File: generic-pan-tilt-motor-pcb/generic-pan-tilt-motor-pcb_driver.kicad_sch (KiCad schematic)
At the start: 19 parts, among them Q1 DMN6075S, U1 TMC5240ATJ+

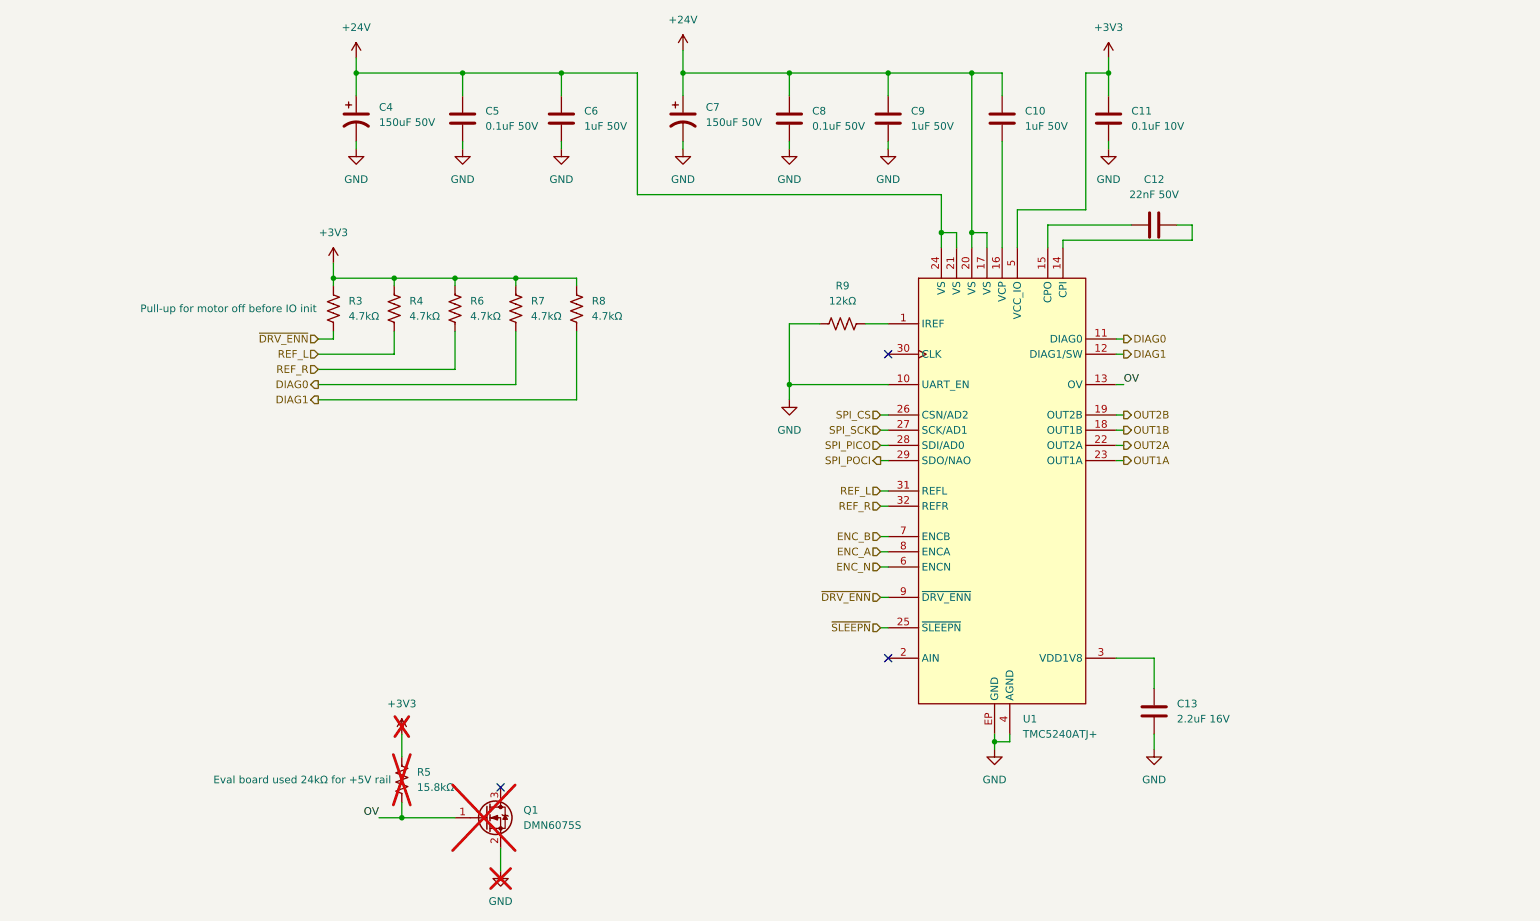
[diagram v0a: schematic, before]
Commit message: motor pcb all footprints, ov circuit
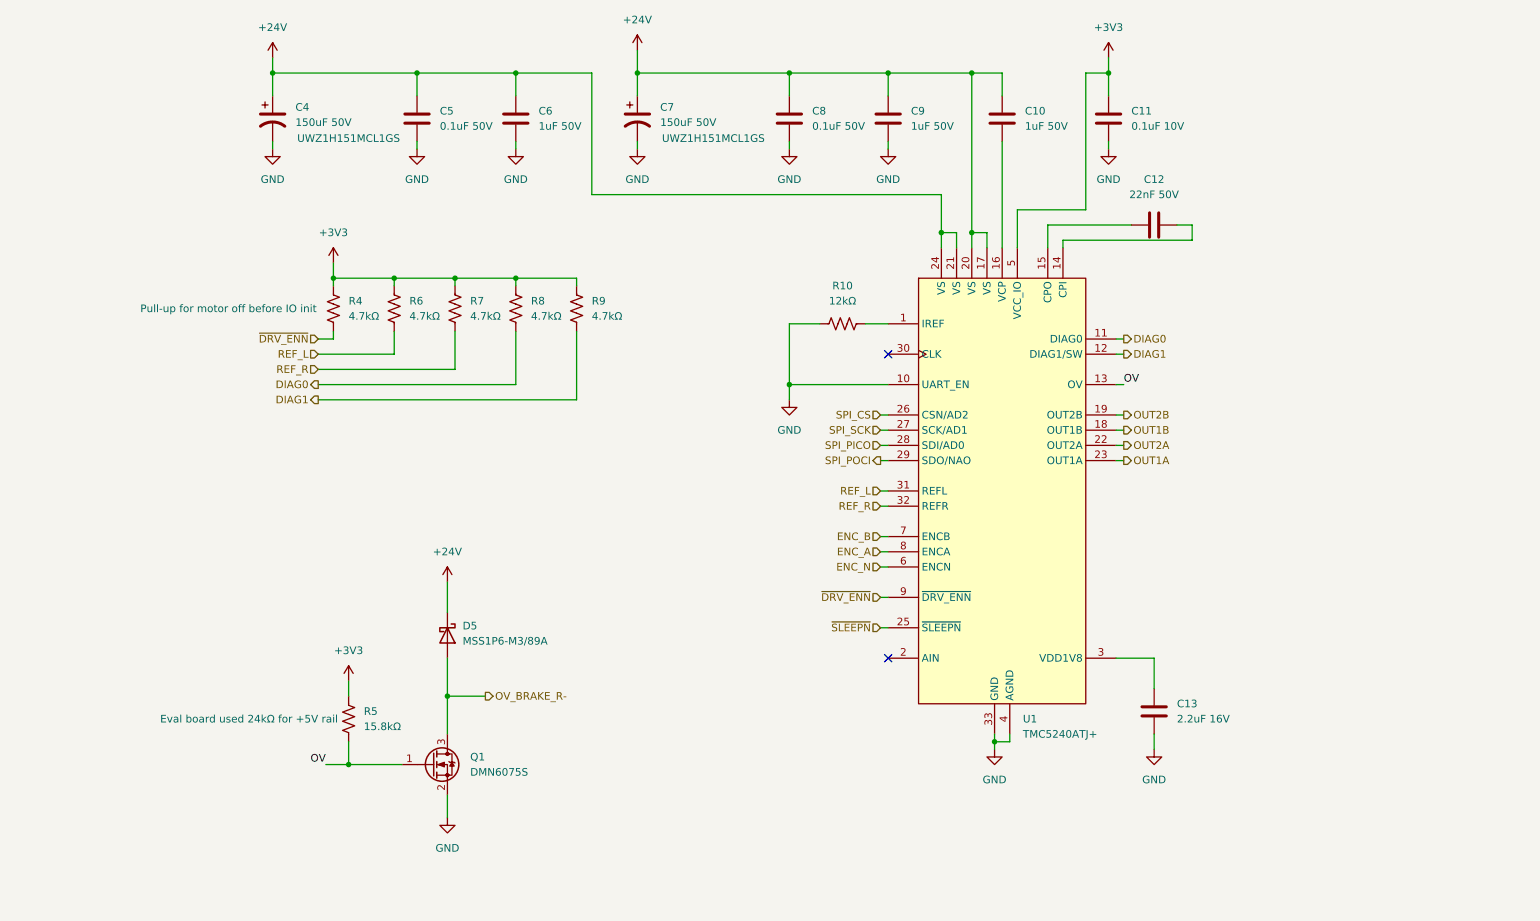
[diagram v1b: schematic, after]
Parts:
- added D5: MSS1P6-M3/89A, Diode_SMD:D_MicroSMP_AK, symbol Device:D_Schottky
- C10, C11, C12, C13, C5, C6, C8, C9: footprint (none) -> Capacitor_SMD:C_0603_1608Metric
- C4, C7: footprint (none) -> Capacitor_SMD:CP_Elec_10x10; digikey# (none) -> 493-9939-1-ND; manf# (none) -> UWZ1H151MCL1GS; mouser# (none) -> 647-UWZ1H151MCL1
- Q1: digikey# (none) -> DMN6075S-7DICT-ND; manf# (none) -> DMN6075S-7; mouser# (none) -> 621-DMN6075S-7; now fitted; now in the parts list
- R10: renamed from R9; footprint (none) -> Resistor_SMD:R_0402_1005Metric
- R4: renamed from R3; footprint (none) -> Resistor_SMD:R_0402_1005Metric
- R5: footprint (none) -> Resistor_SMD:R_0402_1005Metric; now fitted; now in the parts list
- R6: renamed from R4; footprint (none) -> Resistor_SMD:R_0402_1005Metric
- R7: renamed from R6; footprint (none) -> Resistor_SMD:R_0402_1005Metric
- R8: renamed from R7; footprint (none) -> Resistor_SMD:R_0402_1005Metric
- R9: renamed from R8; footprint (none) -> Resistor_SMD:R_0402_1005Metric
- U1: digikey# (none) -> 505-TMC5240ATJ+-ND; manf# (none) -> TMC5240ATJ+; mouser# (none) -> 700-TMC5240ATJ+
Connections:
- net +24V: now also D5.1 (K)
- net GND: now also U1.33 (GND); no longer U1.EP (GND)
- net OV_BRAKE_R-: now reaches Q1.3 (D)
- net OV_BRAKE_R-: now also D5.2 (A)
- no-connect marks 3 -> 2
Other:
- moved on the sheet: C4, C5, C6

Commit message: motor basic layout
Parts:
- added C14, C15, C16, C17: 1nF 100V, Capacitor_SMD:C_0603_1608Metric, symbol Device:C
- C11: value 0.1uF 10V -> 0.1uF 16V
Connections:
- net GND: now also C14.2, C15.2, C16.2, C17.2
- net OUT1A: now also C17.1
- net OUT1B: now also C15.1
- net OUT2A: now also C16.1
- net OUT2B: now also C14.1
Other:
- moved on the sheet: C10, C11, C12, C13, C4, C5, C6, C7, C8, C9, D5, Q1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

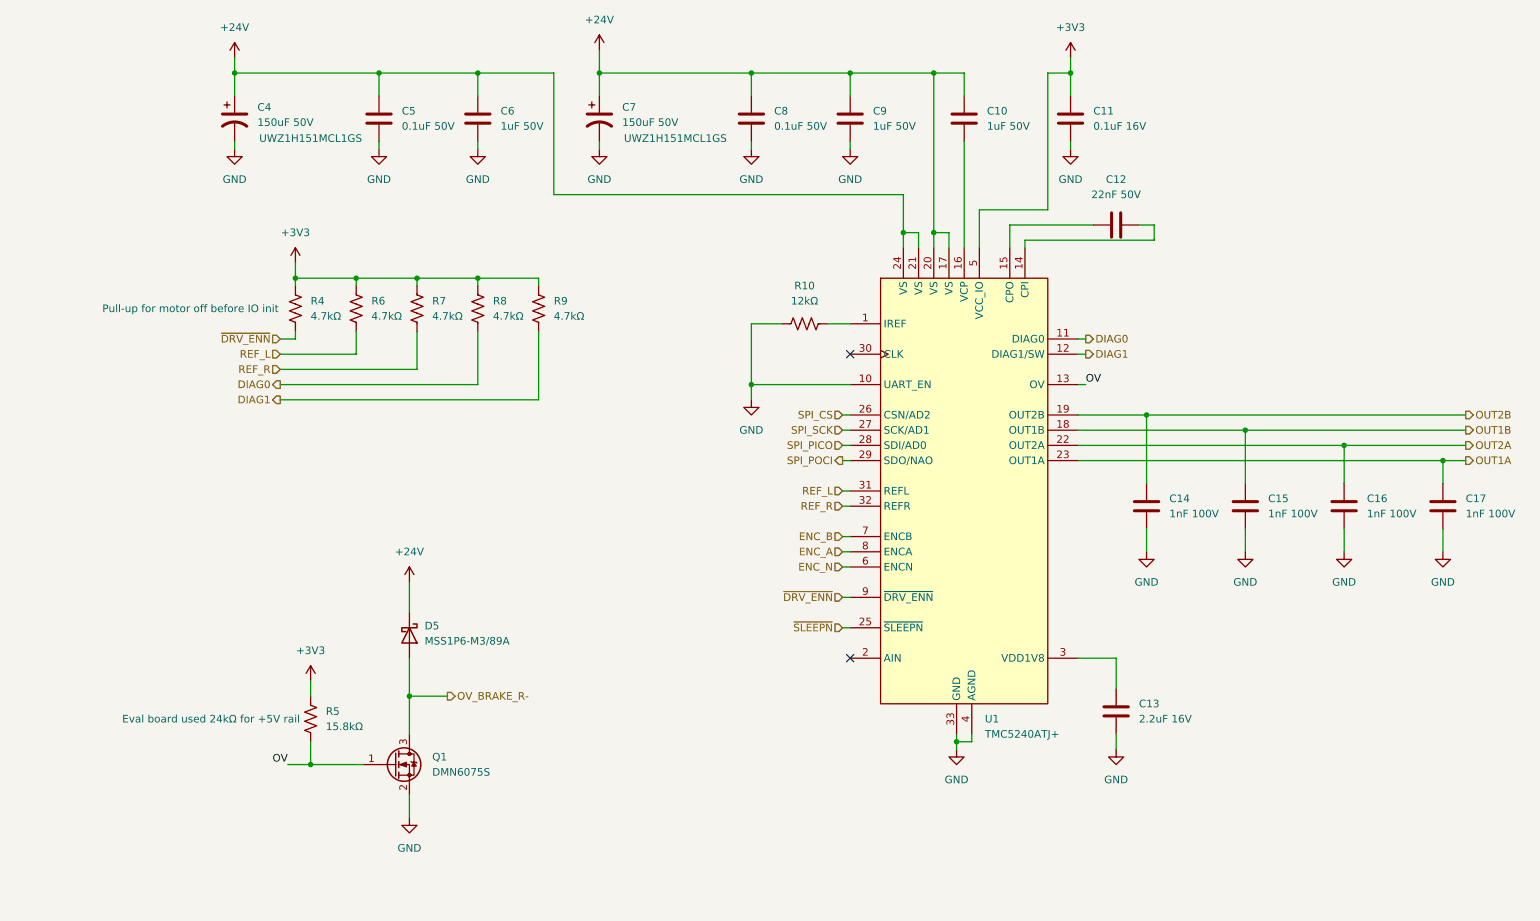
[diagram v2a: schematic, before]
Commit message: fix part numbers, add newark parts, separate fields for part desc
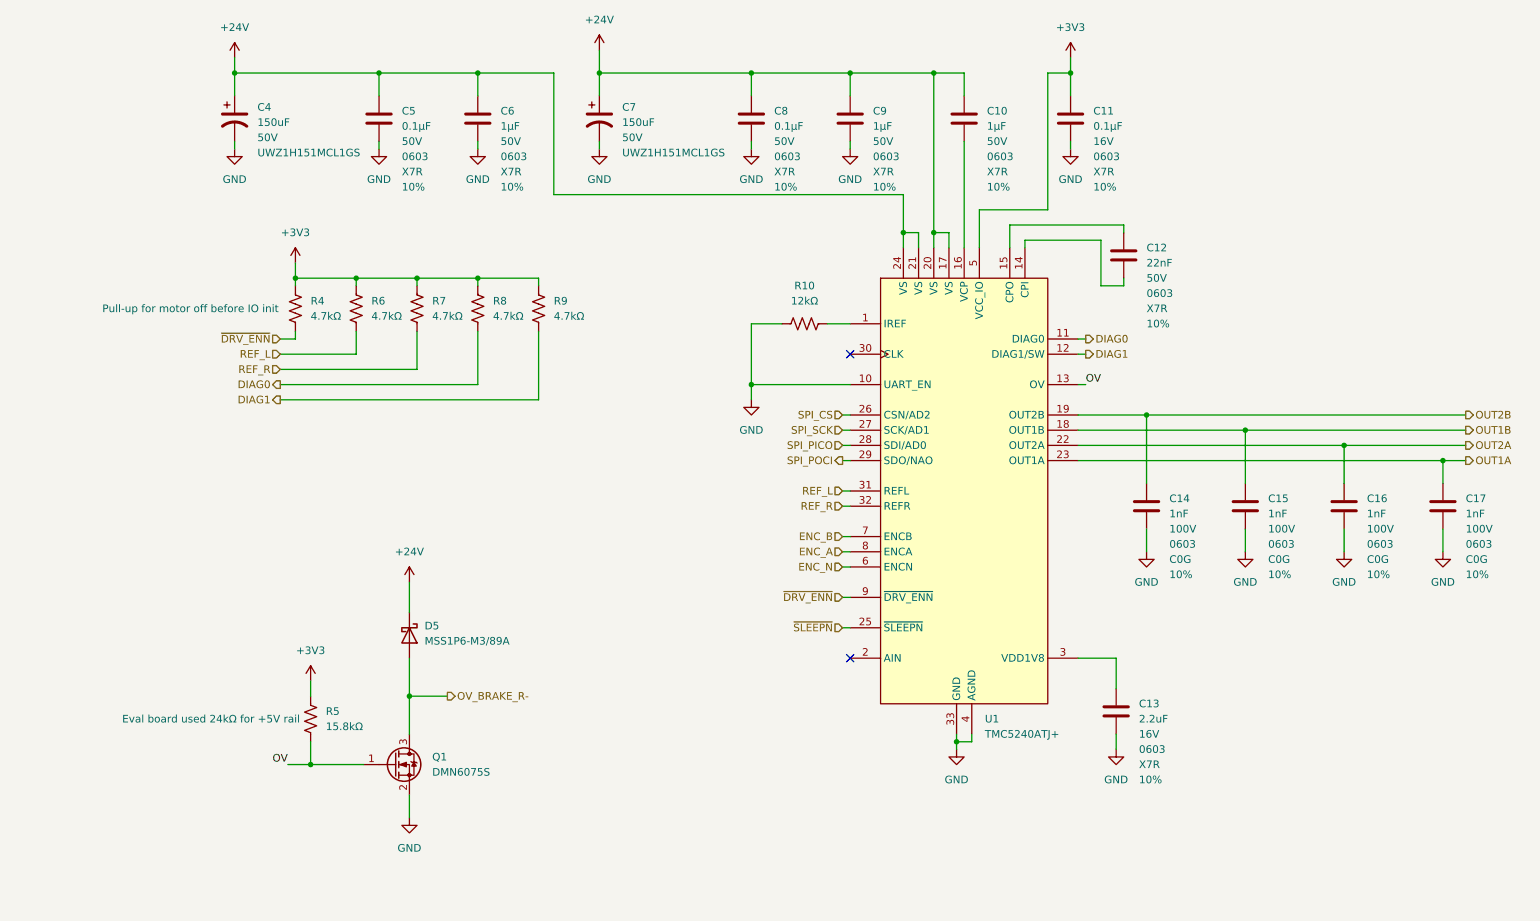
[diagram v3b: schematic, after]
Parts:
- C10, C6, C9: value 1uF 50V -> 1µF; Case Code (none) -> 0603; Dielectric (none) -> X7R; Tolerance (none) -> 10%; Voltage (none) -> 50V; manf# (none) -> CL10B105KB8NQNC; mouser# (none) -> 187­-CL10B105KB8NQNC
- C11: value 0.1uF 16V -> 0.1µF; Case Code (none) -> 0603; Dielectric (none) -> X7R; Tolerance (none) -> 10%; Voltage (none) -> 16V; manf# (none) -> CL10B104KO8NFNC; mouser# (none) -> 187-CL10B104KO8NFNC
- C12: value 22nF 50V -> 22nF; Case Code (none) -> 0603; Dielectric (none) -> X7R; Tolerance (none) -> 10%; Voltage (none) -> 50V; manf# (none) -> CL10B223KB8NNND; mouser# (none) -> 187-CL10B223KB8NNND
- C13: value 2.2uF 16V -> 2.2uF; Case Code (none) -> 0603; Dielectric (none) -> X7R; Tolerance (none) -> 10%; Voltage (none) -> 16V; manf# (none) -> GRM188Z71C225KE43D; mouser# (none) -> 81-­GRM188Z71C225KE3D
- C14, C15, C16, C17: value 1nF 100V -> 1nF; Case Code (none) -> 0603; Dielectric (none) -> C0G; Tolerance (none) -> 10%; Voltage (none) -> 100V; manf# (none) -> C0603C102K1GECTU; mouser# (none) -> 80­-C0603C102K1GEC
- C4, C7: value 150uF 50V -> 150uF; Voltage (none) -> 50V; newark# (none) -> 58R8961
- C5, C8: value 0.1uF 50V -> 0.1µF; Case Code (none) -> 0603; Dielectric (none) -> X7R; Tolerance (none) -> 10%; Voltage (none) -> 50V; manf# (none) -> CL10B104KB8NNNC; mouser# (none) -> 187-­CL10B104KB8NNNC
- D5: newark# (none) -> 75R2576
- Q1: newark# (none) -> 07AH3784
- U1: newark# (none) -> 69AK0101

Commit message: motor fix flipped spi mcp, spi tristate for drc, silk screw terminals, all parts manf and vendors
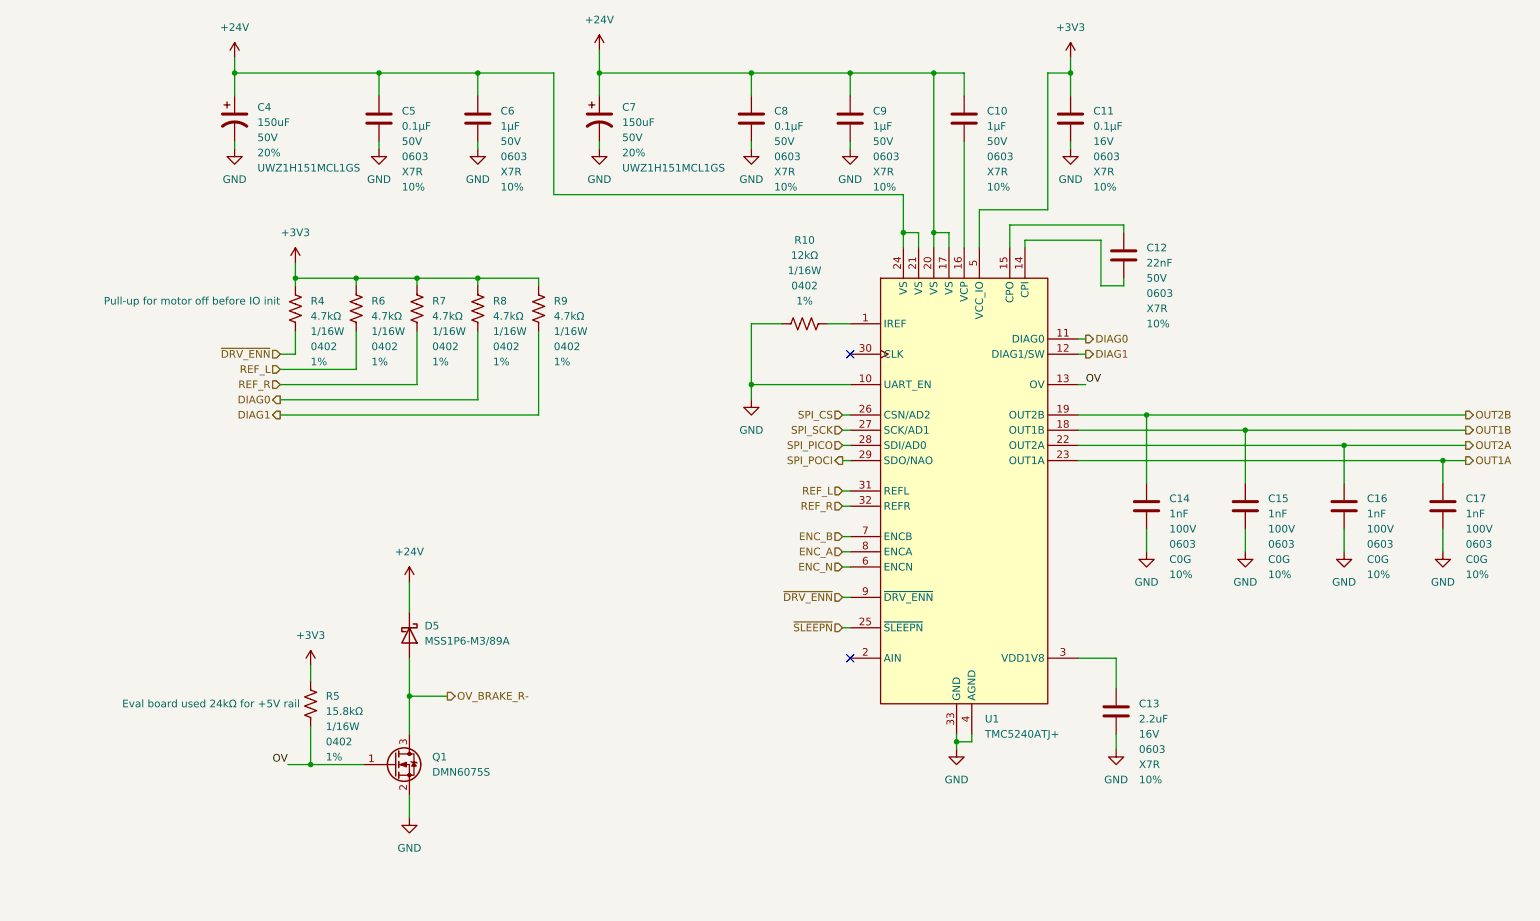
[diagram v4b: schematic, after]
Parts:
- C10, C6, C9: lcsc# (none) -> C5199872
- C11: digikey# (none) -> 1276-1005-1-ND; lcsc# (none) -> C66501; manf# CL10B104KO8NFNC -> CL10B104KO8NNNC; mouser# 187-CL10B104KO8NFNC -> 187-CL10B104KO8NNNC; newark# (none) -> 82AC9325
- C12: digikey# (none) -> 1276-1104-1-ND; lcsc# (none) -> C21122; manf# CL10B223KB8NNND -> CL10B223KB8NNNC; mouser# 187-CL10B223KB8NNND -> 187-CL10B223KB8NNNC; newark# (none) -> 82AC9345
- C13: digikey# (none) -> 490-GRM188Z71C225KE43DCT-ND; lcsc# (none) -> C576485; newark# (none) -> 92AH5122
- C14, C15, C16, C17: digikey# (none) -> 399-17253-1-ND; newark# (none) -> 67AC7933
- C4, C7: Tolerance (none) -> 20%; lcsc# (none) -> C2164473
- C5, C8: digikey# (none) -> 1276-1000-1-ND; lcsc# (none) -> C1591
- D5: lcsc# (none) -> C2927415
- Q1: lcsc# (none) -> C155242
- R10: Case Code (none) -> 0402; Power (none) -> 1/16W; Tolerance (none) -> 1%; digikey# (none) -> CR0402-FX-1202GLFCT-ND; lcsc# (none) -> C2085429; manf# (none) -> CR0402-FX-1202GLF; mouser# (none) -> 652-CR0402FX-1202GLF; newark# (none) -> 33AK7333
- R4, R6, R7, R8, R9: Case Code (none) -> 0402; Power (none) -> 1/16W; Tolerance (none) -> 1%; digikey# (none) -> CR0402-FX-4701GLFCT-ND; lcsc# (none) -> C2076851; manf# (none) -> CR0402-FX-4701GLF; mouser# (none) -> 652-CR0402FX-4701GLF; newark# (none) -> 34AK1324
- R5: Case Code (none) -> 0402; Power (none) -> 1/16W; Tolerance (none) -> 1%; digikey# (none) -> 118-CR0402-FX-1582GLFCT-ND; manf# (none) -> CR0402-FX-1582GLF; mouser# (none) -> 652-CR0402FX1582GLF; newark# (none) -> 40Y9659
- U1: digikey# 505-TMC5240ATJ+-ND -> 175-TMC5240ATJ+TCT-ND; lcsc# (none) -> C7494373; manf# TMC5240ATJ+ -> TMC5240ATJ+T
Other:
- moved on the sheet: R5

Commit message: motor board fix fields, add drc exclusion
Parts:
- R10: mouser# 652-CR0402FX-1202GLF -> 652-CR0402FX-1202GLF
- R4, R6, R7, R8, R9: mouser# 652-CR0402FX-4701GLF -> 652-CR0402FX-4701GLF
- R5: Note (none) -> Eval board used 24kΩ for +5V rail; Notes Eval board used 24kΩ for +5V rail -> (none)
- U1: lcsc# C7494373 -> C7494373
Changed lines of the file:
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@@
 			)
 		)
-		(property "mouser#" "652-CR0402FX-4701GLF "
+		(property "mouser#" "652-CR0402FX-4701GLF"
 			(at 100.33 72.39 0)
 			(effects
@@
 			)
 		)
-		(property "Notes" "Eval board used 24kΩ for +5V rail"
+		(property "Note" "Eval board used 24kΩ for +5V rail"
 			(at 60.452 138.43 0)
 			(effects
@@
 			)
 		)
-		(property "mouser#" "652-CR0402FX-1202GLF "
+		(property "mouser#" "652-CR0402FX-1202GLF"
 			(at 144.78 74.93 0)
 			(effects
@@
 			)
 		)
-		(property "mouser#" "652-CR0402FX-4701GLF "
+		(property "mouser#" "652-CR0402FX-4701GLF"
 			(at 90.17 72.39 0)
 			(effects
@@
 			)
 		)
-		(property "lcsc#" " C7494373"
+		(property "lcsc#" "C7494373"
 			(at 171.45 102.87 0)
 			(effects
@@
 			)
 		)
-		(property "mouser#" "652-CR0402FX-4701GLF "
+		(property "mouser#" "652-CR0402FX-4701GLF"
 			(at 80.01 72.39 0)
 			(effects
@@
 			)
 		)
-		(property "mouser#" "652-CR0402FX-4701GLF "
+		(property "mouser#" "652-CR0402FX-4701GLF"
 			(at 59.69 72.39 0)
 			(effects
@@
 			)
 		)
-		(property "mouser#" "652-CR0402FX-4701GLF "
+		(property "mouser#" "652-CR0402FX-4701GLF"
 			(at 69.85 72.39 0)
 			(effects
